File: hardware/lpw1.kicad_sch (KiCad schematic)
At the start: 12 parts, among them J7 JST PH2P ST, Q2 DMG2305UXQ-7, U9 MCP73831-2

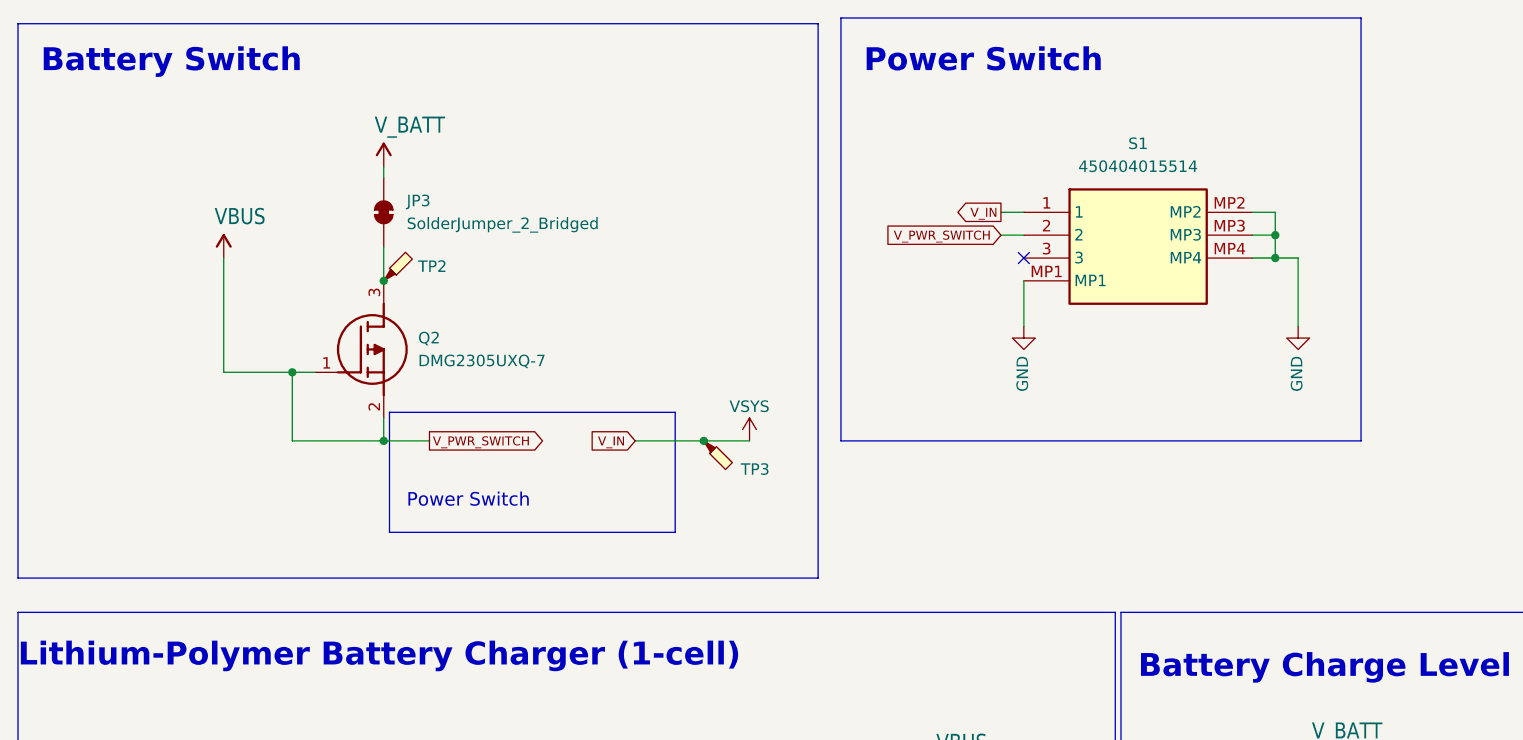
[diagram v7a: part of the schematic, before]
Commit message: removed short between Mosfet G/S, some other minor changes
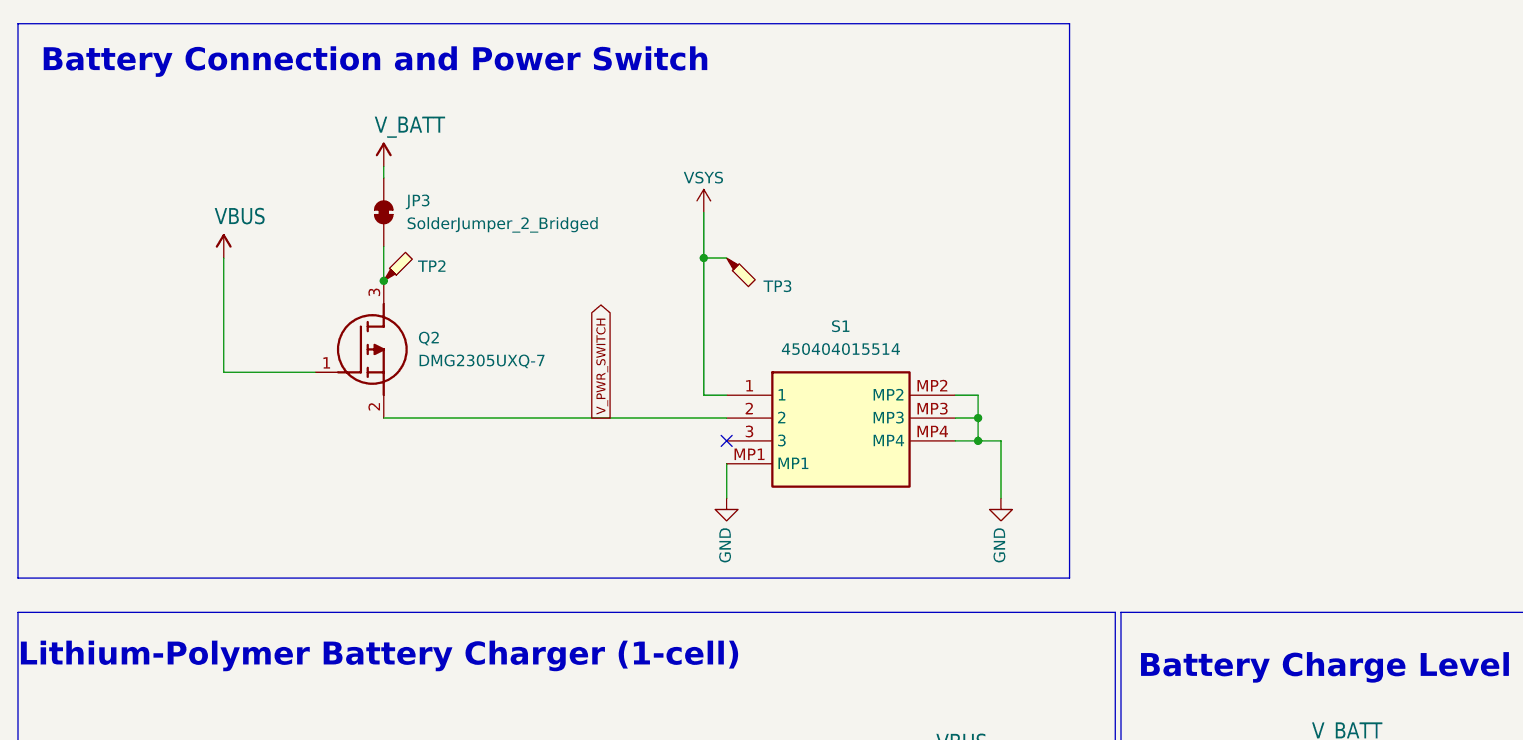
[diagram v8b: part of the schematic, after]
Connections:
- net VBUS: no longer Q2.2 (S), S1.2
- new net V_PWR_SWITCH: Q2.2 (S), S1.2
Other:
- note added: "Battery Connection and Power Switch"
- note removed: "Battery Switch"
- note removed: "Power Switch"
- moved on the sheet: S1, TP3
